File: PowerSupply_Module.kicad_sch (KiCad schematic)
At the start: 21 parts, among them J9 Battery, U13 MC34063AD, U4 BQ24075RGT

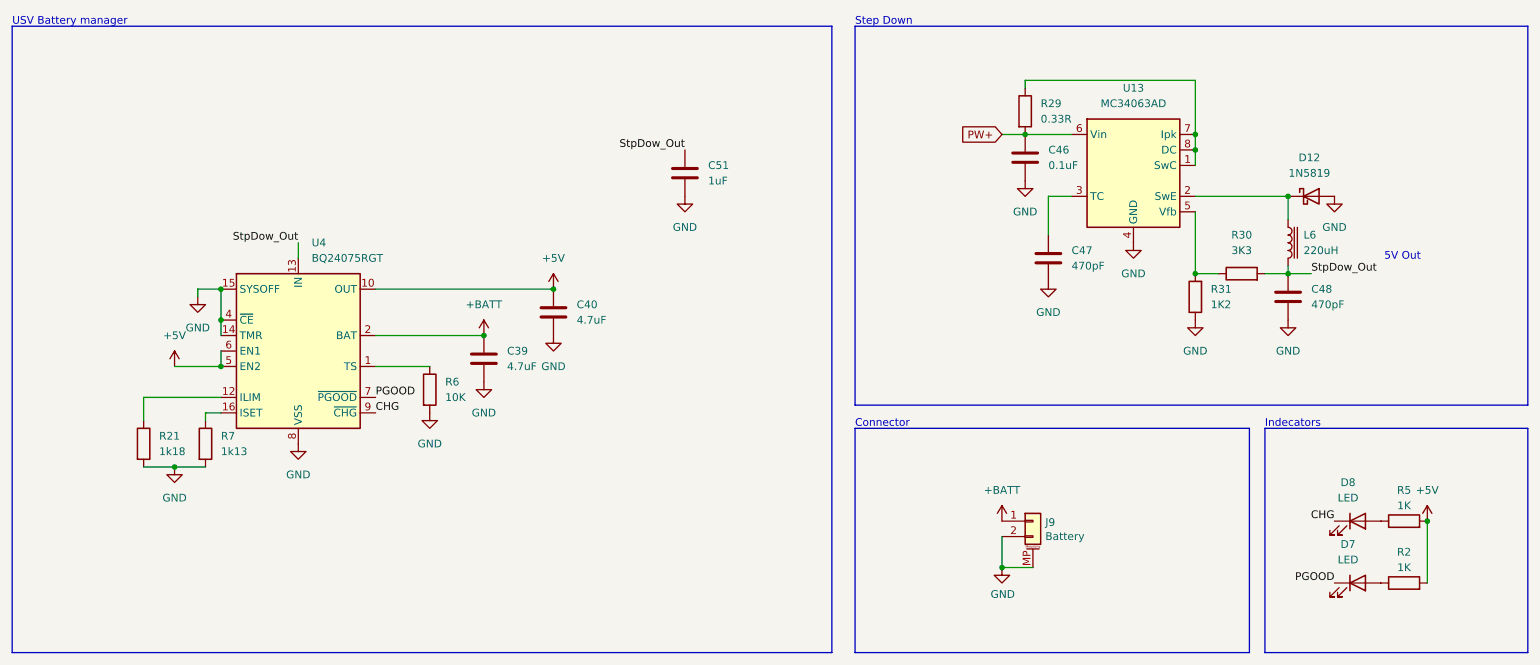
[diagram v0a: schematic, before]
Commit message: updated schematics:
Fixed bug with PWKEY of LTE module

Fixed big with power
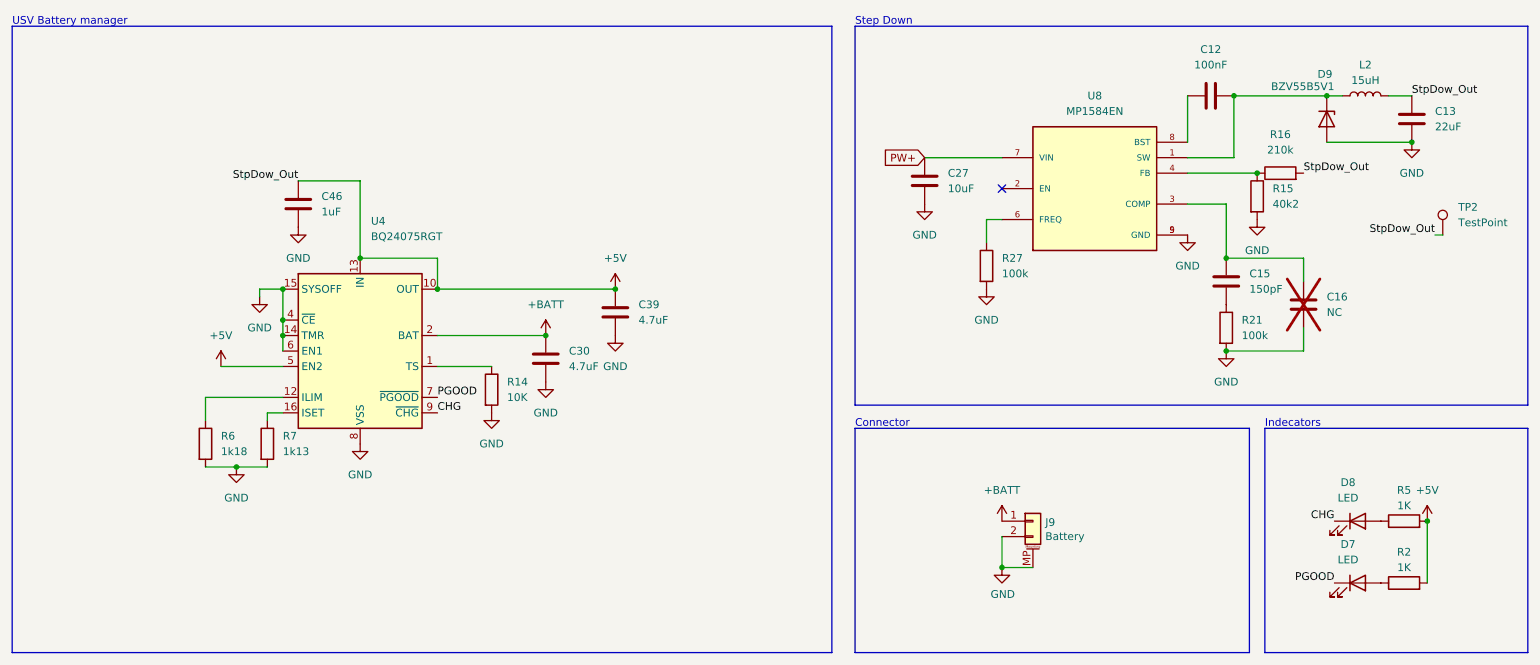
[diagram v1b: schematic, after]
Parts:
- removed C40: 4.7uF, Capacitor_SMD:C_0805_2012Metric, symbol Device:C
- removed C47, C48: 470pF, Capacitor_SMD:C_0603_1608Metric, symbol Device:C
- removed C51: 1uF, Capacitor_SMD:C_0603_1608Metric, symbol Device:C
- removed D12: 1N5819, Diode_SMD:D_SOD-123, symbol Diode:1N5819
- removed L6: 220uH, Inductor_SMD:L_7.3x7.3_H4.5, symbol Device:L_Iron
- removed R29: 0.33R, Resistor_SMD:R_0603_1608Metric, symbol Device:R
- removed R30: 3K3, Resistor_SMD:R_0603_1608Metric, symbol Device:R
- removed R31: 1K2, Resistor_SMD:R_0603_1608Metric, symbol Device:R
- removed U13: MC34063AD, Package_SO:SOIC-8_3.9x4.9mm_P1.27mm, symbol Regulator_Switching:MC34063AD
- added C12: 100nF, symbol Device:C
- added C13: 22uF, symbol Device:C
- added C15: 150pF, symbol Device:C
- added C16: NC, symbol Device:C
- added C27: 10uF, symbol Device:C
- added C30: 4.7uF, Capacitor_SMD:C_0805_2012Metric, symbol Device:C
- added D9: BZV55B5V1, Diode_SMD:D_MiniMELF, symbol Diode:BZV55B5V1
- added L2: 15uH, symbol Device:L
- added R14: 10K, Resistor_SMD:R_0603_1608Metric, symbol Device:R
- added R15: 40k2, symbol Device:R
- added R16: 210k, symbol Device:R
- added R27: 100k, symbol Device:R
- added TP2: TestPoint, symbol Connector:TestPoint
- added U8: MP1584EN, SOIC127P600X170-9N:SOIC127P600X170-9N, symbol MP1584EN:MP1584EN
- C46: value 0.1uF -> 1uF; footprint Capacitor_SMD:C_0805_2012Metric -> Capacitor_SMD:C_0603_1608Metric
- R21: value 1k18 -> 100k; footprint Resistor_SMD:R_0603_1608Metric -> (none)
- R6: value 10K -> 1k18
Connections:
- net StpDow_Out is gone; now on net +5V: U4.13 (IN)
- net +5V: now also C39.1, C46.1, C13.1, L2.2, R16.2, TP2.1; no longer U4.6 (EN1)
- net +BATT: now also C30.1; no longer C39.1
- net GND: now also U4.6 (EN1), C13.2, C16.1, C27.1, C30.2, D9.2 (A), R14.2, R15.2, R27.2, U8.5 (GND), U8.9 (GND)
- net PW+: now also C27.2, U8.7 (VIN); no longer C46.1
- net at R21.1: now also C15.1; no longer U4.12 (ILIM)
- net at R6.1: now also U4.12 (ILIM); no longer U4.1 (TS)
- new net: C15.2, C16.2, U8.3 (COMP)
- new net: C12.2, D9.1 (K), L2.1, U8.1 (SW)
- new net: R15.1, R16.1, U8.4 (FB)
- new net: R27.1, U8.6 (FREQ)
- new net: C12.1, U8.8 (BST)
- new net: R14.1, U4.1 (TS)
- no-connect marks 0 -> 1
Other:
- note removed: "5V Out"

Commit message: first new layout
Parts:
- C12, C16: footprint (none) -> Capacitor_SMD:C_0805_2012Metric
- C13, C15: footprint (none) -> Capacitor_SMD:C_0603_1608Metric
- C27: footprint (none) -> Capacitor_SMD:C_1206_3216Metric
- L2: footprint (none) -> Inductor_SMD:L_Abracon_ASPI-0630LR
- R15: value 40k2 -> 40K2; footprint (none) -> Resistor_SMD:R_0603_1608Metric
- R16: value 210k -> 210K; footprint (none) -> Resistor_SMD:R_0603_1608Metric
- R21, R27: value 100k -> 100K; footprint (none) -> Resistor_SMD:R_0603_1608Metric
- TP2: footprint (none) -> TestPoint:TestPoint_Pad_D1.5mm
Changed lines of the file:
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@@
 			)
 		)
-		(property "Footprint" ""
+		(property "Footprint" "Capacitor_SMD:C_0603_1608Metric"
 			(at 213.6648 54.61 0)
 			(effects
@@
 			)
 		)
-		(property "Footprint" ""
+		(property "Footprint" "Inductor_SMD:L_Abracon_ASPI-0630LR"
 			(at 237.49 27.94 0)
 			(effects
@@
 			)
 		)
-		(property "Footprint" ""
+		(property "Footprint" "Capacitor_SMD:C_0603_1608Metric"
 			(at 246.0752 35.56 0)
 			(effects
@@
 			)
 		)
-		(property "Value" "210k"
+		(property "Value" "210K"
 			(at 223.52 36.83 90)
 			(effects
@@
 			)
 		)
-		(property "Footprint" ""
+		(property "Footprint" "Resistor_SMD:R_0603_1608Metric"
 			(at 223.52 42.418 90)
 			(effects
@@
 			)
 		)
-		(property "Footprint" ""
+		(property "Footprint" "Capacitor_SMD:C_0805_2012Metric"
 			(at 226.3648 58.42 0)
 			(effects
@@
 			)
 		)
-		(property "Value" "100k"
+		(property "Value" "100K"
 			(at 217.17 67.3099 0)
 			(effects
@@
 			)
 		)
-		(property "Footprint" ""
+		(property "Footprint" "Resistor_SMD:R_0603_1608Metric"
 			(at 212.852 66.04 90)
 			(effects
@@
 			)
 		)
-		(property "Footprint" ""
+		(property "Footprint" "TestPoint:TestPoint_Pad_D1.5mm"
 			(at 255.27 50.8 0)
 			(effects
@@
 			)
 		)
-		(property "Footprint" ""
+		(property "Footprint" "Capacitor_SMD:C_0805_2012Metric"
 			(at 215.9 26.9748 0)
 			(effects
@@
 			)
 		)
-		(property "Footprint" ""
+		(property "Footprint" "Capacitor_SMD:C_1206_3216Metric"
 			(at 164.1348 38.1 0)
 			(effects
@@
 			)
 		)
-		(property "Value" "40k2"
+		(property "Value" "40K2"
 			(at 222.25 45.7199 0)
 			(effects
@@
 			)
 		)
-		(property "Footprint" ""
+		(property "Footprint" "Resistor_SMD:R_0603_1608Metric"
 			(at 217.932 44.45 90)
 			(effects
@@
 			)
 		)
-		(property "Value" "100k"
+		(property "Value" "100K"
 			(at 177.8 57.1499 0)
 			(effects
@@
 			)
 		)
-		(property "Footprint" ""
+		(property "Footprint" "Resistor_SMD:R_0603_1608Metric"
 			(at 173.482 55.88 90)
 			(effects

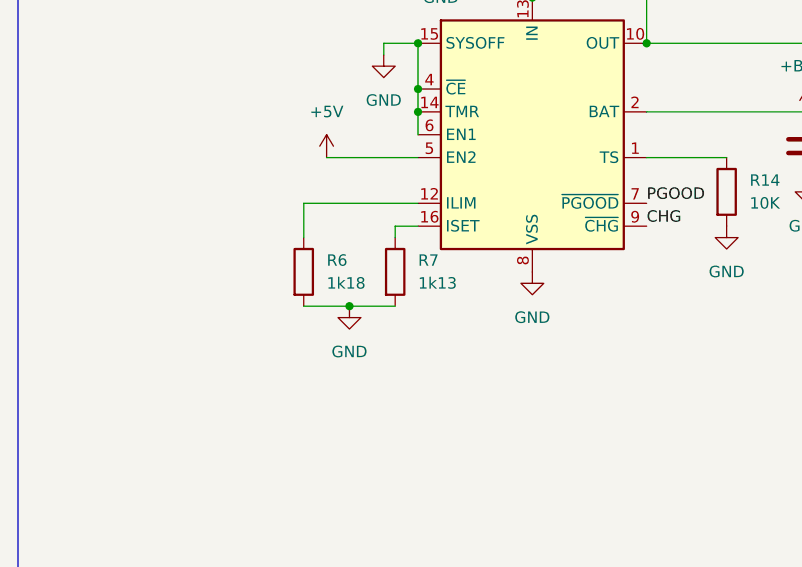
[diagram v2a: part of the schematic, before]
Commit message: cahnged resistor value for charing current
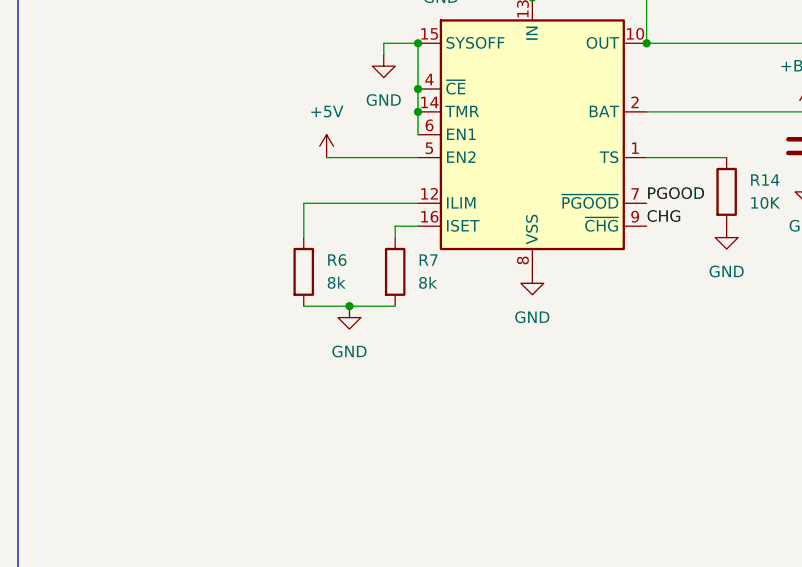
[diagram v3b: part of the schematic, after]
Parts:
- R6: value 1k18 -> 8k
- R7: value 1k13 -> 8k
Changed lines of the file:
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@@
 			)
 		)
-		(property "Value" "1k13"
+		(property "Value" "8k"
 			(at 59.69 86.3599 0)
 			(effects
@@
 			)
 		)
-		(property "Value" "1k18"
+		(property "Value" "8k"
 			(at 49.53 86.3599 0)
 			(effects
